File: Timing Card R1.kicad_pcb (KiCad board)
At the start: 4 copper layers, 65 x 40.5 mm, 139 parts, among them J1 71430-0101, J10 10018784-10201TLF, J2 Conn_01x10, U1 LCMXO2-7000HC-6TG144I, U10 74AHC125, U11 T602-025.0M, U12 FM24C64B, U2 SN74LVC1G125DRL, U3 74AHCT125, U4 74AHCT125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

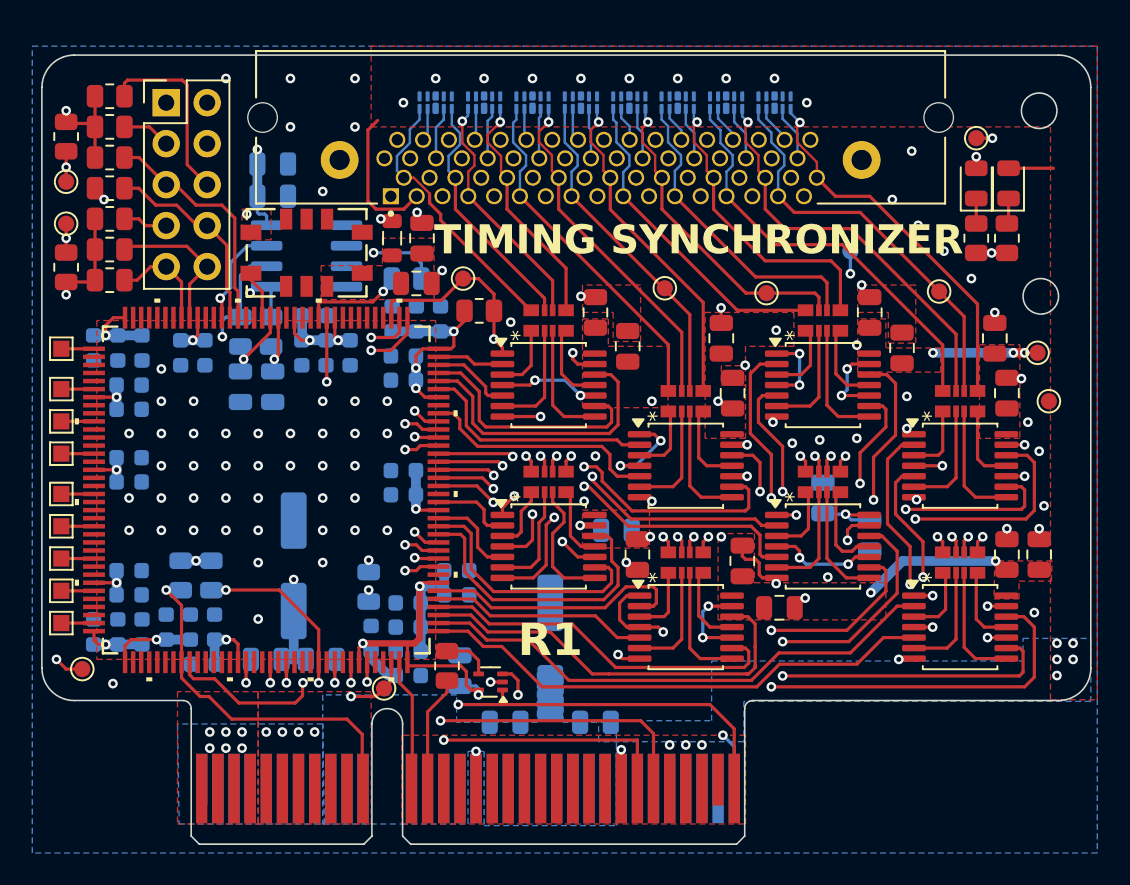
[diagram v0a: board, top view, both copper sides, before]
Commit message: Fixed board size
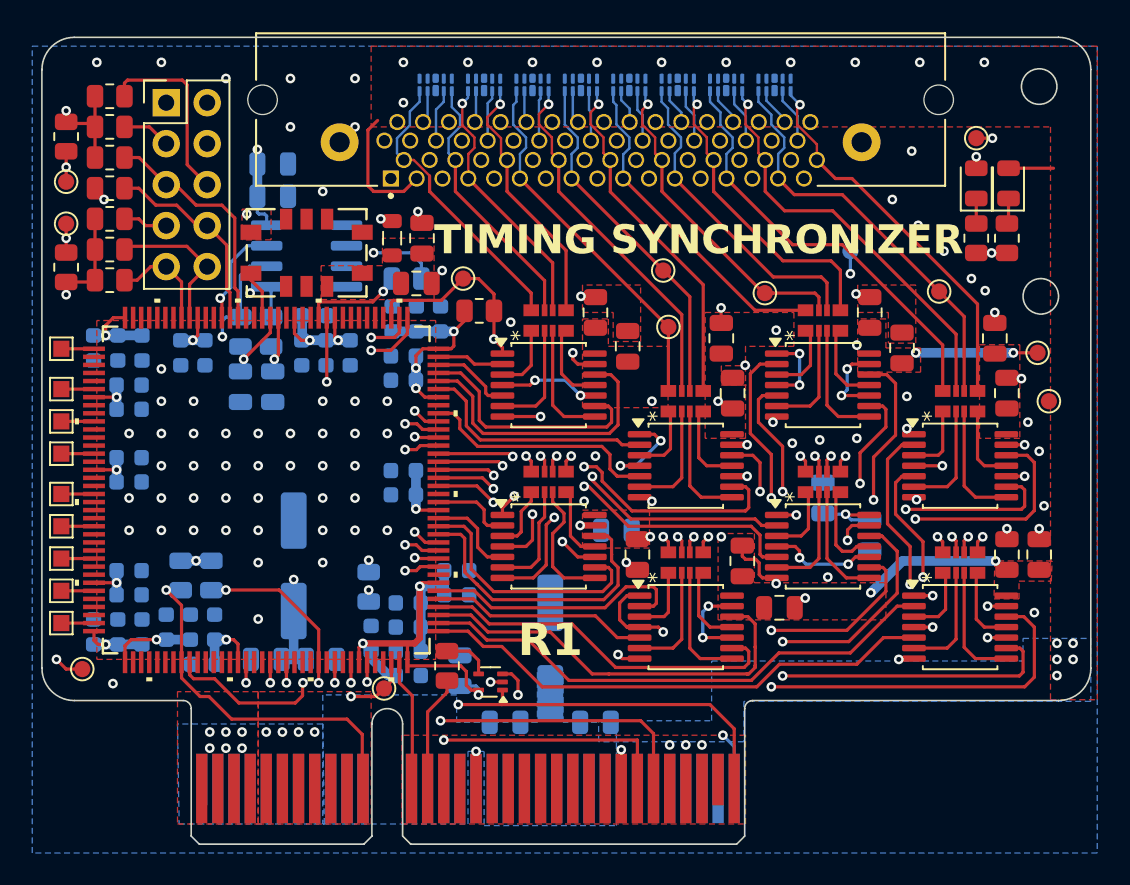
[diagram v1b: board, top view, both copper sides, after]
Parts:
- added TP22: TestPoint, TestPoint:TestPoint_Pad_D1.0mm, F.Cu at (66.4, 70.4)
- moved TP17 1.10 mm to (66.1, 66.9)
- moved D1 1.10 mm to (55.0, 55.4)
- moved D2 1.10 mm to (58.0, 55.4)
- moved D3 1.10 mm to (61.0, 55.4)
- moved D4 1.10 mm to (64.0, 55.4)
- moved D5 1.10 mm to (52.0, 55.4)
- moved D6 1.10 mm to (67.0, 55.4)
- moved D7 1.10 mm to (70.0, 55.4)
- moved D8 1.10 mm to (73.0, 55.4)
- moved J1 1.10 mm to (62.2, 59.5)
- moved TP18 0.10 mm to (72.4, 68.3)
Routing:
- net /3V3_OUT0: track 16.9 -> 18.0 mm
- net /5V_OUT9: track 27.7 -> 28.8 mm
- net /5V_OUT1: track 26.0 -> 27.1 mm
- net /3V3_OUT6: track 21.0 -> 22.1 mm
- net /3V3_OUT4: track 21.9 -> 23.0 mm
- net /3V3_OUT2: track 15.6 -> 16.7 mm
- net /5V_OUT7: track 31.2 -> 32.3 mm
- net /5V_OUT5: track 31.7 -> 32.8 mm
- net /5V_OUT4: track 32.5 -> 33.6 mm
- net /5V_OUT3: track 25.4 -> 26.5 mm
- net /5V_OUT2: track 25.7 -> 26.8 mm
- net /5V_OUT14: track 33.8 -> 34.9 mm
- net /5V_OUT13: track 33.7 -> 34.8 mm
- net /5V_OUT12: track 34.2 -> 35.3 mm
- net /5V_OUT11: track 27.3 -> 28.4 mm
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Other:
- board size 65 x 40.5 mm -> 65 x 41.6 mm
